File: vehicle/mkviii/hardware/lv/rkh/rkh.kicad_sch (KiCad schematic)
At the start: 67 parts, among them J1 TWO_WIRE_SCREW_TERMINAL, J2 TWO_WIRE_SCREW_TERMINAL, J3 J_PCIe_x1, J4 TWO_WIRE_SCREW_TERMINAL, J5 J_Programming_Pin_Header, J7 Conn_01x03_Pin, J8 Conn_01x02_Pin, U2 Roadkill_MCU, U4 MCP2561-E-SN, Y1 Crystal_16MHz_18pF

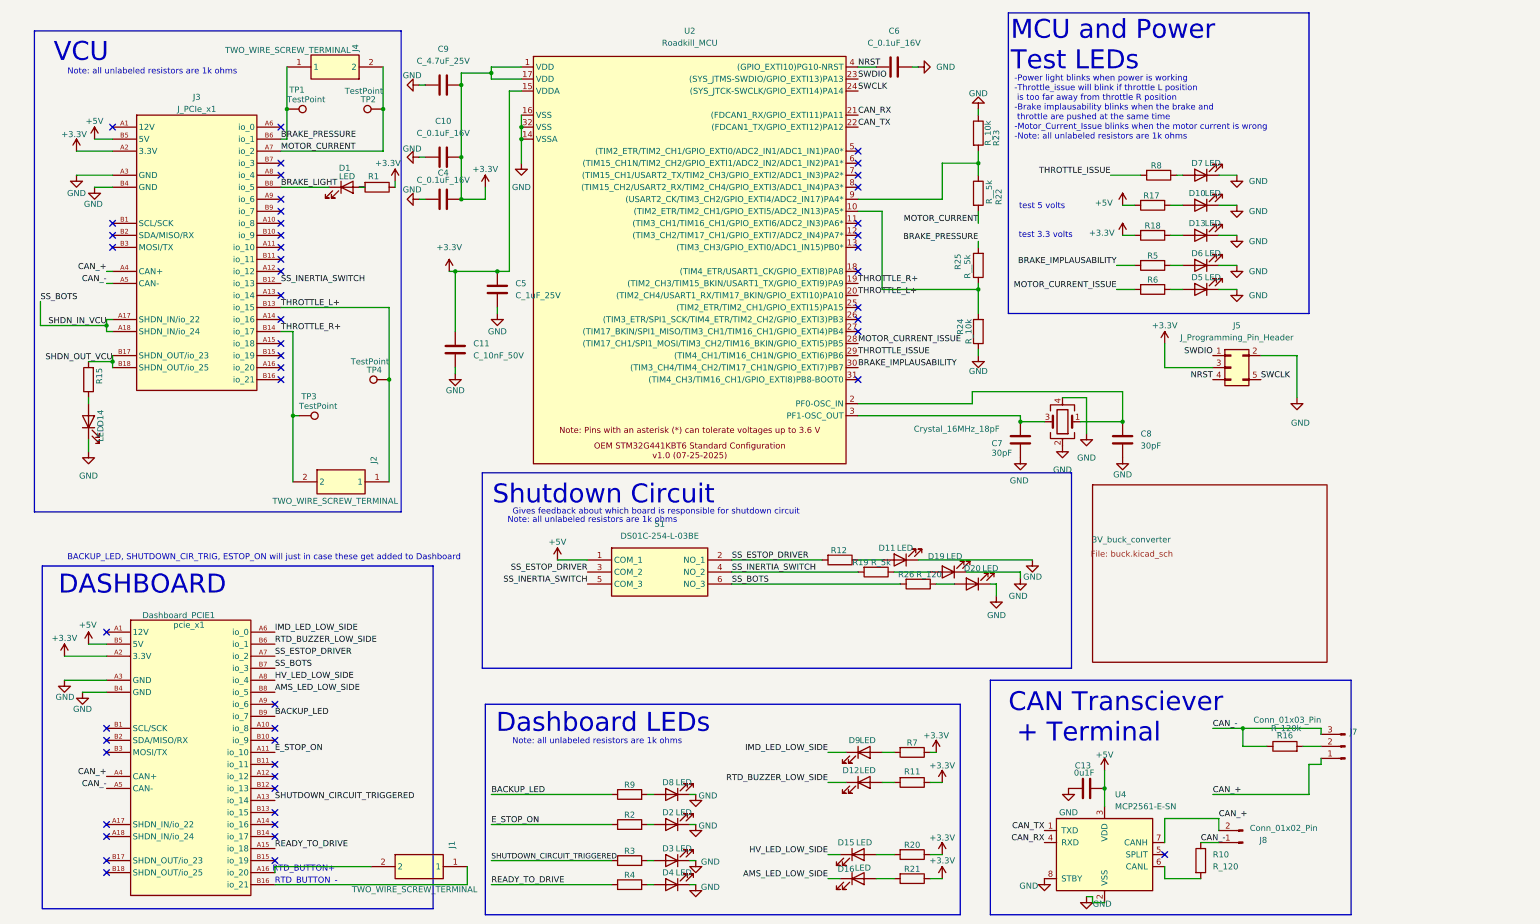
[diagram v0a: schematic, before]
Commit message: Added production files; rounded corners; added throttle power wire terminal
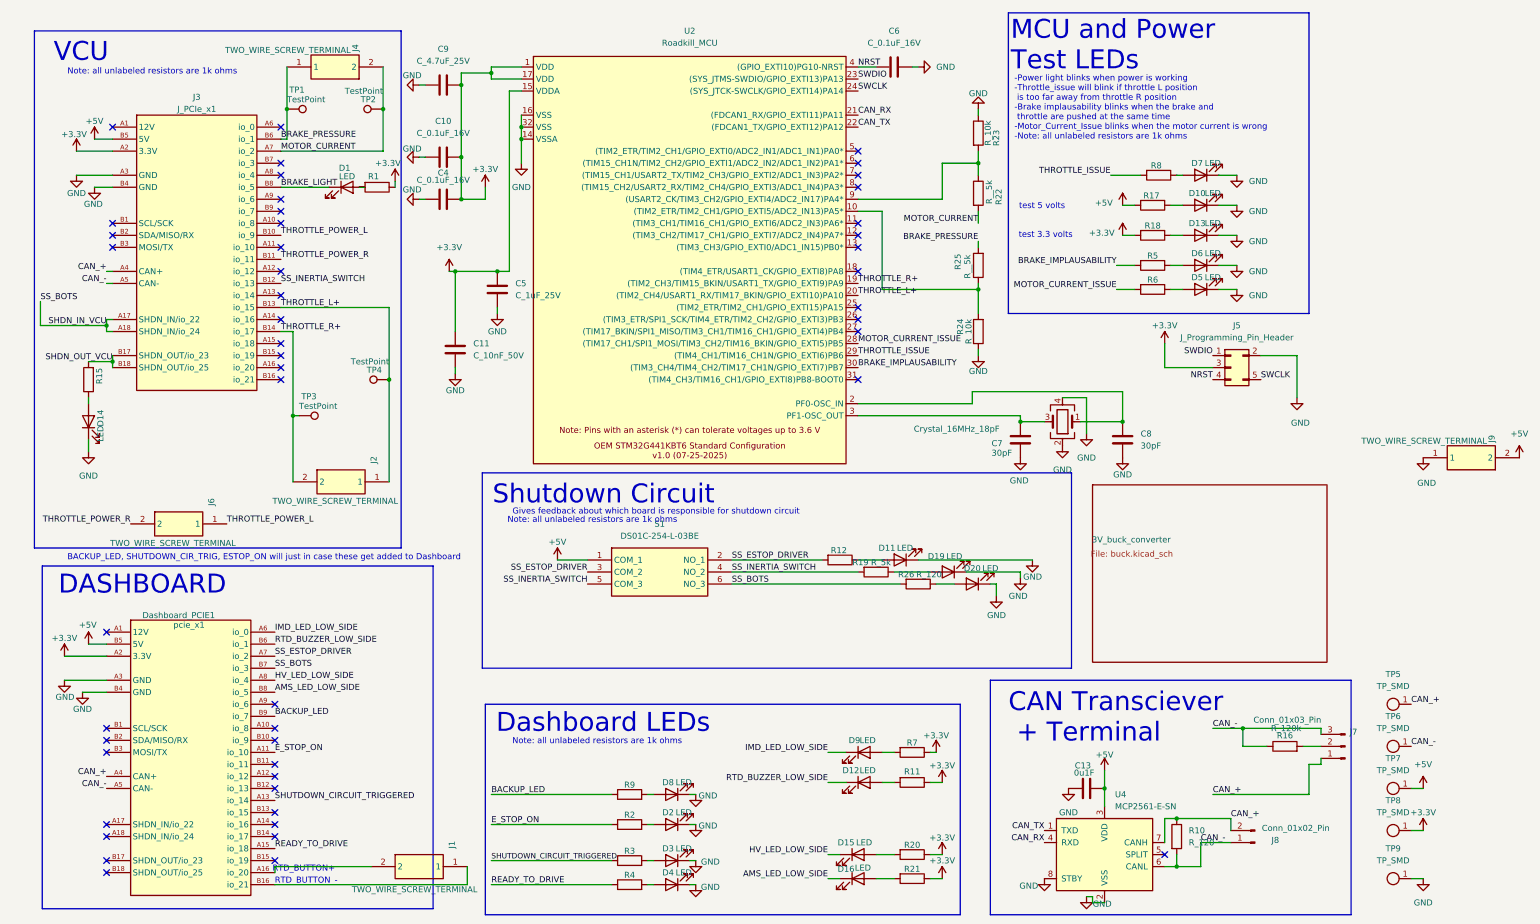
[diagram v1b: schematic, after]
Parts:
- added J6, J9: TWO_WIRE_SCREW_TERMINAL, OEM:wire_terminal_delete_asap, symbol 691412320002:TWO_WIRE_SCREW_TERMINAL
- added TP5, TP6, TP7, TP8, TP9: TP_SMD, OEM:TP_Hook_SMD, symbol OEM:TP_Hook_SMD
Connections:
- net +3.3V: now also TP8.1
- net +5V: now also J9.2, TP7.1
- net CAN_+: now also R10.1, TP5.1
- net CAN_-: now also R10.2, U4.6 (CANL), TP6.1; no longer R10.1
- net GND: now also J9.1, TP9.1
- net THROTTLE_POWER_L: now reaches J3.B10 (io_9)
- net THROTTLE_POWER_L: now also J6.1
- net THROTTLE_POWER_R: now reaches J3.B11 (io_11)
- net THROTTLE_POWER_R: now also J6.2
- no-connect marks 51 -> 49
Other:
- title: (none) -> Roadkill Harness (LV Only)
- moved on the sheet: J8, R10
